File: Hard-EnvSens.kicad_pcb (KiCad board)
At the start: 2 copper layers, 60 x 76.6 mm, 86 parts, among them J2 Conn_01x04_Socket, J3 Conn_02x02_Odd_Even, J4 Conn_01x04_Pin, J5 Conn_02x02_Odd_Even, J6 Conn_01x02_Pin, Q1 SS8050, Q2 SS8050, SW1 SW_Push, U10 BMI160, U3 IP5306, U4 VEML7700-TR, U5 DPS368, U6 SGP41-D-R4, U7 SHT40-AD1B-R2, U8 AS7341-DLGT

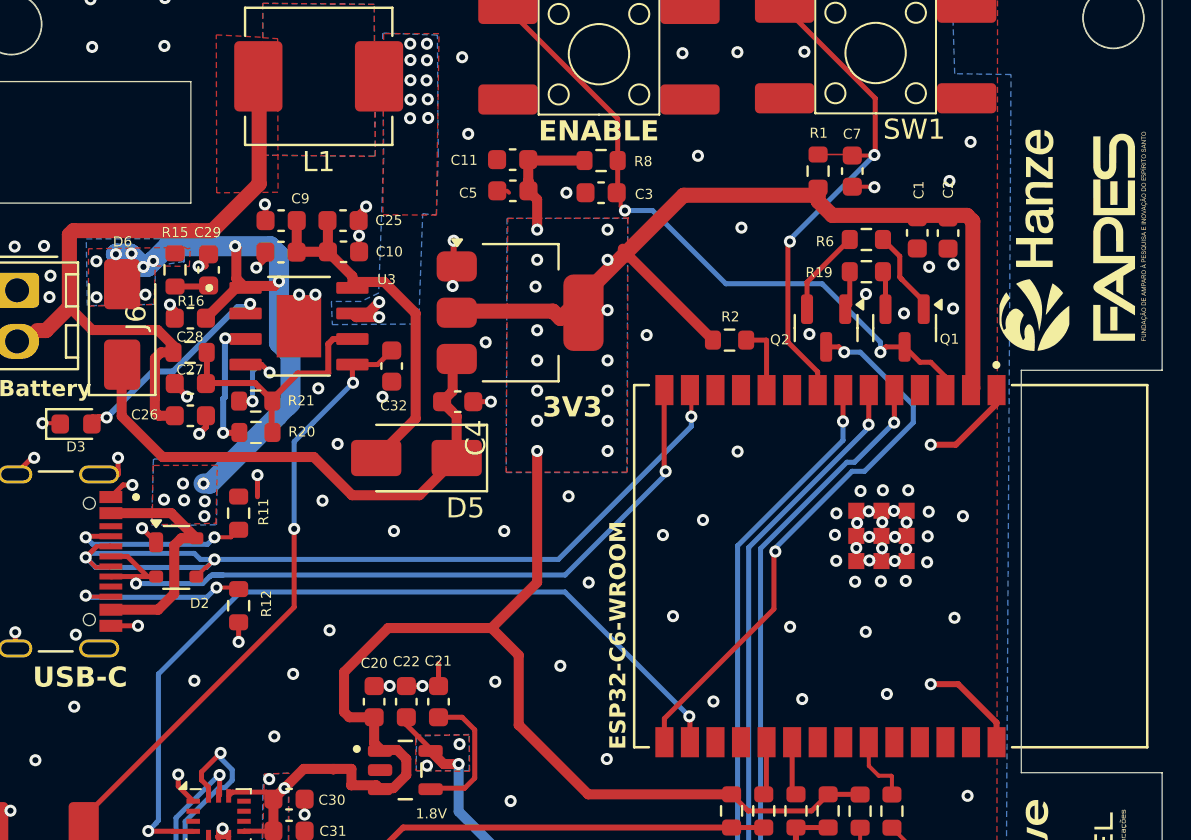
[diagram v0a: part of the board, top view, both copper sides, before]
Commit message: New charger + 3v3 Switch
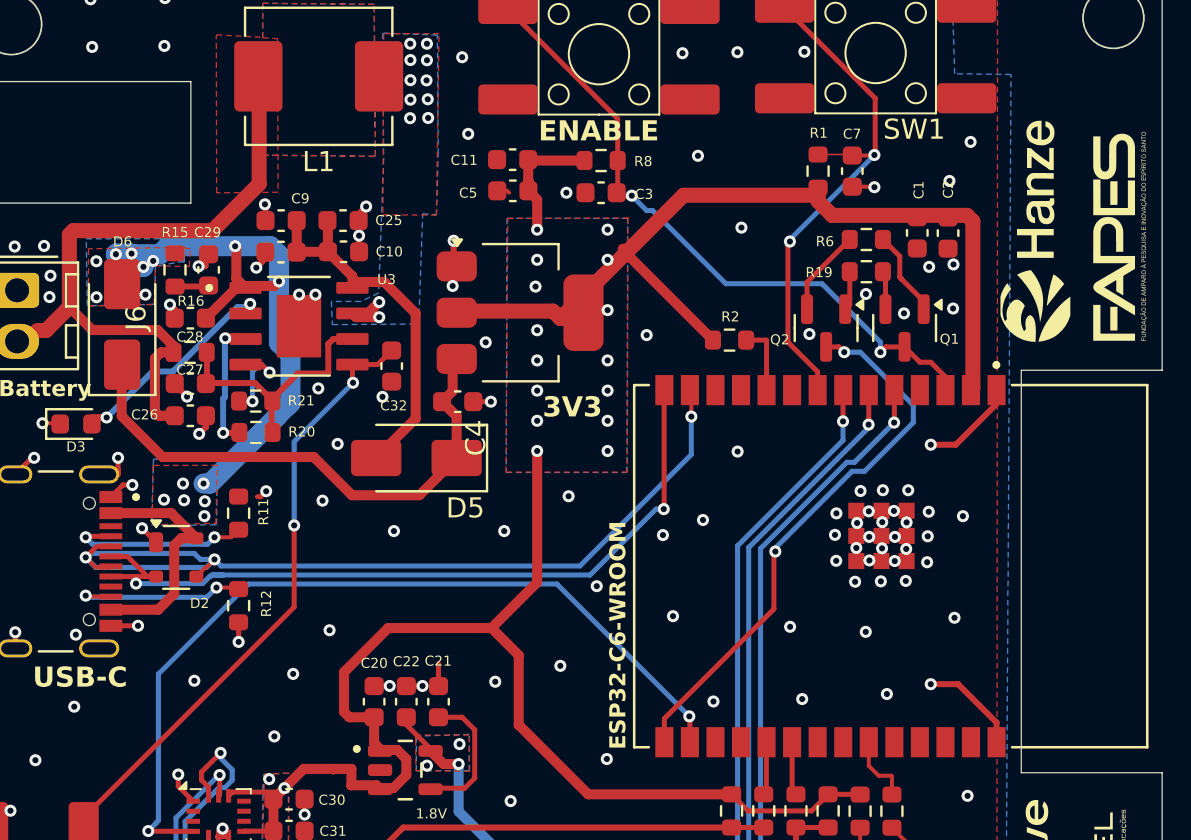
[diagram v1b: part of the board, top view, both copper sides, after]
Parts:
- moved G*** 0.45 mm to (153.8, 63.3)
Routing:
- net +5V: track 41.9 -> 43.2 mm
- net D-: track 46.0 -> 47.1 mm
- net D+: track 38.7 -> 39.6 mm
- net GND: track 42.9 -> 42.4 mm

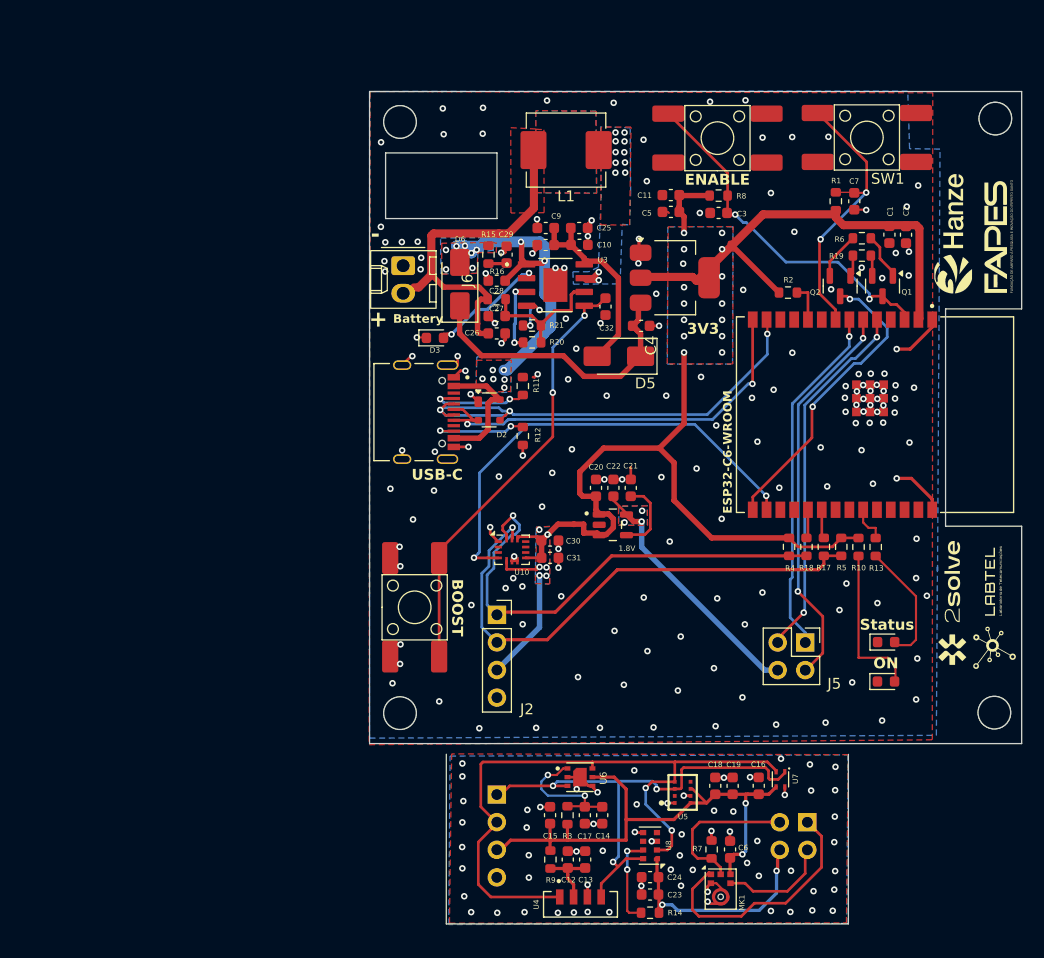
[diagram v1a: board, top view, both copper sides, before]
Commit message: small changes + gotta fix the charger
Maybe rotating the charger 2 gets a better pin configuration
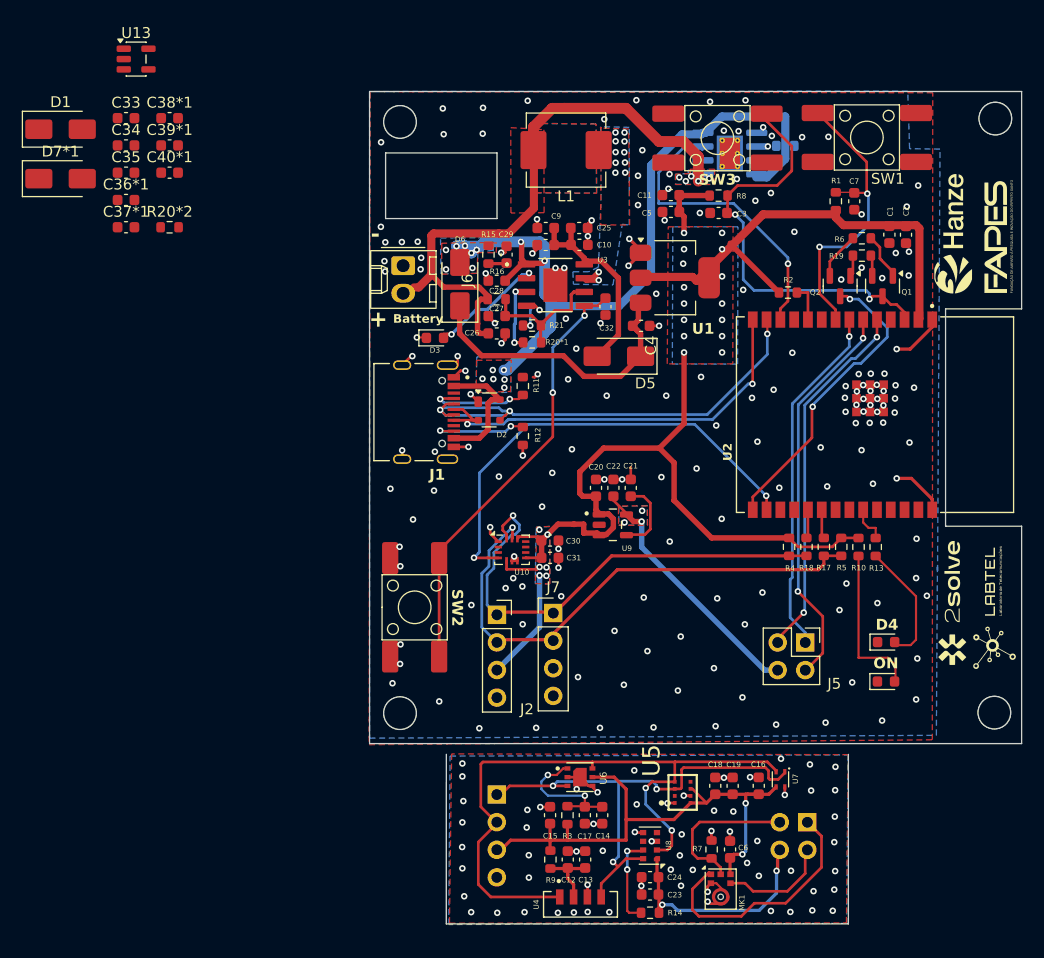
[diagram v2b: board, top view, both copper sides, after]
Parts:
- added C33: 1uF, Capacitor_SMD:C_0603_1608Metric, F.Cu at (77.7, 52.6)
- added C34: 0.1uF, Capacitor_SMD:C_0603_1608Metric, F.Cu at (77.7, 55.2)
- added C35: 1nF, Capacitor_SMD:C_0603_1608Metric, F.Cu at (77.7, 57.7)
- added C36*1: 10uF, Capacitor_SMD:C_0603_1608Metric, F.Cu at (77.7, 60.2)
- added C37*1: 10uF, Capacitor_SMD:C_0603_1608Metric, F.Cu at (77.7, 62.7)
- added C38*1: 10nF, Capacitor_SMD:C_0603_1608Metric, F.Cu at (81.7, 52.6)
- added C39*1: 100uF, Capacitor_SMD:C_0603_1608Metric, F.Cu at (81.7, 55.2)
- added C40*1: 10uF, Capacitor_SMD:C_0603_1608Metric, F.Cu at (81.7, 57.7)
- added D1: SS14, Diode_SMD:D_SMA, F.Cu at (71.7, 53.7)
- added D7*1: SS14, Diode_SMD:D_SMA, F.Cu at (71.7, 58.2)
- added J7: Conn_01x04_Pin, Connector_PinHeader_2.54mm:PinHeader_1x04_P2.54mm_Vertical, F.Cu at (117.0, 98.2)
- added R10*1: 1.2k, Resistor_SMD:R_0603_1608Metric, B.Cu at (138.3, 55.2)
- added R20*2: 0R, Resistor_SMD:R_0603_1608Metric, F.Cu at (81.7, 62.7)
- added U12*1: TP4056-42-ESOP8, Package_SO:SOIC-8-1EP_3.9x4.9mm_P1.27mm_EP2.41x3.3mm_ThermalVias, B.Cu at (133.2, 55.9)
- added U13: SPX3819M5-L-3-3, Package_TO_SOT_SMD:SOT-23-5, F.Cu at (78.6, 47.2)
- U5: footprint Biblioteca_Kicad:LGA8S145X65P2X4_200X250X110-V -> libs:LGA8S145X65P2X4_200X250X110-V
- renumbered Status to D4, USB-C to J1, R20 to R20*1, BOOST to SW2, ENABLE to SW3, 3V3 to U1, ESP32-C6-WROOM to U2, 1.8V to U9
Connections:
- net Net-(J6-Pin_2) renamed Bat+
- C20 pad 1: +3V3 -> 3v3_aux
- C30 pad 1: +3V3 -> 3v3_aux
- C31 pad 1: +3V3 -> 3v3_aux
- J2 pad 3: +3V3 -> 3v3_aux
- R4 pad 2: +3V3 -> 3v3_aux
- R5 pad 2: +3V3 -> 3v3_aux
- SW2 pad 3: Net-(U3-KEY) -> (no net)
- SW2 pad 4: GND -> (no net)
- SW3 pad 3: (no net) -> EN
- U10 pad 5: +3V3 -> 3v3_aux
- U10 pad 8: +3V3 -> 3v3_aux
- U2 pad 12: unconnected-(U2-GPIO11-Pad12) -> Charge_Bat
- U2 pad 17: unconnected-(U2-GPIO19-Pad17) -> Sensors_3v3
- U2 pad 29_1: GND -> (no net)
- U2 pad 29_2: GND -> (no net)
- U2 pad 29_3: GND -> (no net)
- U2 pad 29_4: GND -> (no net)
- U2 pad 29_5: GND -> (no net)
- U2 pad 29_6: GND -> (no net)
- U2 pad 29_7: GND -> (no net)
- U2 pad 29_8: GND -> (no net)
- U2 pad 29_9: GND -> (no net)
- U9 pad 1: +3V3 -> 3v3_aux
- U9 pad 3: +3V3 -> 3v3_aux
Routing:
- net +5V: track 43.2 -> 85.3 mm
- net Charge_Bat: track 0.00 -> 27.9 mm, vias 0 -> 1
- net Bat+: track 32.6 -> 54.7 mm, vias 0 -> 5
- net +3V3: track 129.4 -> 115.1 mm, vias 21 -> 20
- net 3v3_aux: track 0.00 -> 14.3 mm, vias 0 -> 1
- net EN: track 32.8 -> 39.6 mm
- net Net-(U2-GPIO0/ADC1_CH0/XTAL_32K_P): track 26.5 -> 28.2 mm
- net Net-(U12*1-PROG): track 0.00 -> 1.03 mm, vias 0 -> 1
- net GND: track 42.4 -> 42.1 mm, vias 162 -> 172
- added copper zone on B.Cu, net Bat+

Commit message: Almost finished board
New 3v3 regulaator
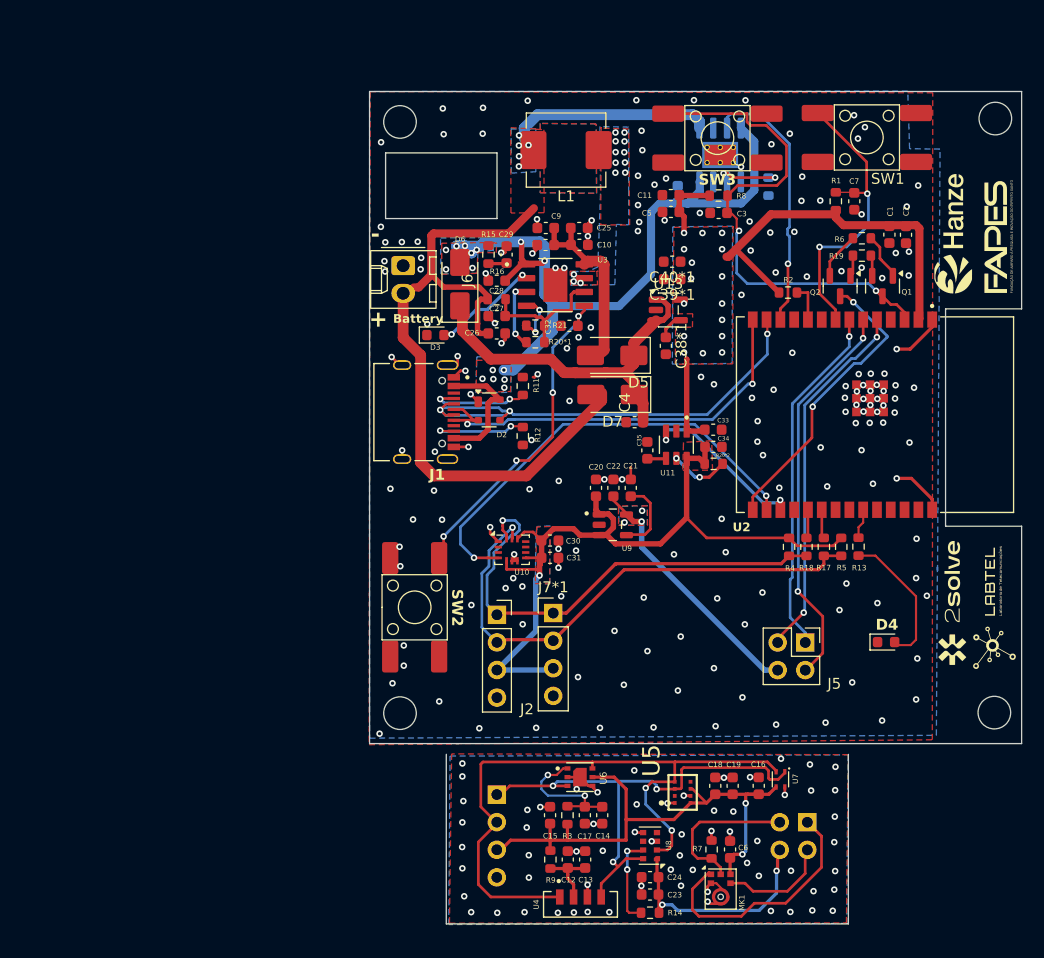
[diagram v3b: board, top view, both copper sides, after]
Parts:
- removed C37*1: 10uF, Capacitor_SMD:C_0603_1608Metric
- removed D1, D7*1: SS14, Diode_SMD:D_SMA
- removed ON: LED, LED_SMD:LED_0603_1608Metric
- removed R10: 1K, Resistor_SMD:R_0603_1608Metric
- removed U1: LD1117S33TR_SOT223, Package_TO_SOT_SMD:SOT-223-3_TabPin2
- added D7: CMS30I30A, Diode_SMD:D_SMA, F.Cu at (122.5, 78.1)
- added U11: TPS22918TDBVRQ1, libs:SOT95P280X145-6N, F.Cu at (128.3, 82.7)
- C36*1: moved to B.Cu
- D5, D6: value SS14 -> CMS30I30A
- moved C33 61.2 mm to (131.7, 81.3)
- moved C34 60.8 mm to (131.7, 82.9)
- moved R20*2 54.6 mm to (131.8, 84.5)
- moved C35 54.4 mm to (125.7, 83.2), turned to 90 degrees
- moved U13 54.1 mm to (127.6, 70.3)
- moved C36*1 50.8 mm to (128.5, 59.6), turned to 90 degrees
- moved C38*1 50.2 mm to (127.4, 73.6), turned to -90 degrees
- moved C39*1 47.9 mm to (128.0, 67.5), turned to 180 degrees
- moved C40*1 47.0 mm to (127.9, 65.9), turned to 180 degrees
- moved C4 8.89 mm to (124.5, 80.6), turned to 180 degrees
- moved R10*1 4.06 mm to (136.8, 59.0), turned to -90 degrees
- moved C32 3.76 mm to (118.5, 71.8), turned to 180 degrees
- moved R13 1.58 mm to (145.1, 92.1)
- moved U12*1 0.90 mm to (132.4, 56.0), turned to 90 degrees
- moved D5 0.62 mm to (122.4, 74.5)
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- renumbered J7 to J7*1
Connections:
- C33 pad 1: Net-(D1-K) -> +3V3
- C39*1 pad 1: 3v3_regulator2 -> +3V3
- C40*1 pad 1: 3v3_regulator2 -> +3V3
- J7*1 pad 2: GND -> Scl
- J7*1 pad 3: Scl -> 3v3_aux
- J7*1 pad 4: +3V3 -> GND
- SW3 pad 3: EN -> (no net)
- U10 pad 12: +3V3 -> 3v3_aux
- U13 pad 1: Bat+ -> Net-(D5-K)
- U13 pad 3: Bat+ -> Net-(D5-K)
- U13 pad 5: 3v3_regulator2 -> +3V3
- U2 pad 29_1: (no net) -> GND
- U2 pad 29_2: (no net) -> GND
- U2 pad 29_3: (no net) -> GND
- U2 pad 29_4: (no net) -> GND
- U2 pad 29_5: (no net) -> GND
- U2 pad 29_6: (no net) -> GND
- U2 pad 29_7: (no net) -> GND
- U2 pad 29_8: (no net) -> GND
- U2 pad 29_9: (no net) -> GND
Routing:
- net +3V3: track 115.1 -> 49.4 mm, vias 20 -> 16
- net 3v3_aux: track 14.3 -> 72.8 mm
- net Bat+: track 54.7 -> 82.7 mm
- net Sensors_3v3: track 0.00 -> 16.1 mm, vias 0 -> 2
- net Net-(D1-A): track 14.5 -> 0.00 mm
- net Net-(U3-KEY): track 40.1 -> 31.1 mm, vias 2 -> 4
- net EN: track 39.6 -> 47.5 mm
- net Net-(D5-K): track 28.6 -> 34.5 mm
- net +5V: track 85.3 -> 79.5 mm
- net GND: track 42.1 -> 36.4 mm, vias 172 -> 175
- net Net-(U11-QOD): track 0.00 -> 5.48 mm, vias 0 -> 2
- net Net-(U12*1-PROG): track 1.03 -> 6.14 mm, vias 1 -> 2
- net Charge_Bat: track 27.9 -> 24.7 mm
- net Net-(U3-SW): track 2.98 -> 0.00 mm, vias 12 -> 13
- net Net-(U13-BP): track 0.00 -> 2.47 mm
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- added copper zone on B.Cu, net 3v3_aux
- added copper zone on F.Cu, net 3v3_aux

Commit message: Almost ready to fabricate
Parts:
- added R32*1: 10k, Resistor_SMD:R_0603_1608Metric, B.Cu at (140.1, 62.6)
- C39: renamed from C39*1; footprint Capacitor_SMD:C_0603_1608Metric -> Capacitor_SMD:C_Elec_6.3x7.7
- C40: renamed from C40*1; value 10uF -> 0.1uF
- R31*1: renamed from R10*1; value 1.2k -> 4k
- moved C39 7.83 mm to (129.7, 75.1), turned to -90 degrees
- moved C38 3.29 mm to (126.9, 70.3), turned to 180 degrees
- moved U13 2.57 mm to (127.4, 67.7)
- moved C40 0.62 mm to (127.9, 65.2)
- moved J7*1 0.18 mm to (117.0, 98.4)
- renumbered C38*1 to C38, R20*2 to R30*1
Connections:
- U2 pad 29_1: GND -> (no net)
- U2 pad 29_2: GND -> (no net)
- U2 pad 29_3: GND -> (no net)
- U2 pad 29_4: GND -> (no net)
- U2 pad 29_5: GND -> (no net)
- U2 pad 29_6: GND -> (no net)
- U2 pad 29_7: GND -> (no net)
- U2 pad 29_8: GND -> (no net)
- U2 pad 29_9: GND -> (no net)
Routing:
- net GND: track 36.4 -> 30.0 mm, vias 175 -> 253
- net +3V3: track 49.4 -> 51.9 mm, vias 16 -> 17
- net Net-(D5-K): track 34.5 -> 36.7 mm
- net Net-(U11-QOD): track 5.48 -> 7.54 mm
- net 3v3_aux: track 72.8 -> 74.6 mm
- net Charge_Bat: track 24.7 -> 25.9 mm
- net GND2: vias 64 -> 76
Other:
- outline, holes or cut-outs redrawn
- board text added: "STATUS"

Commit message: ready to fabricate
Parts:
- added 1V8: TestPoint, TestPoint:TestPoint_THTPad_1.5x1.5mm_Drill0.7mm, F.Cu at (149.3, 106.6)
- added 3V3: TestPoint, TestPoint:TestPoint_THTPad_1.5x1.5mm_Drill0.7mm, F.Cu at (145.5, 103.5)
- added ?: , , F.Cu at (157.6, 107.3)
- added ?: , , F.Cu at (102.9, 53.0)
- added ?: , , F.Cu at (102.9, 107.4)
- added Bat: TestPoint, TestPoint:TestPoint_THTPad_1.5x1.5mm_Drill0.7mm, F.Cu at (145.5, 106.7)
- added Boost: TestPoint, TestPoint:TestPoint_THTPad_1.5x1.5mm_Drill0.7mm, F.Cu at (145.5, 100.3)
- added GND: TestPoint, TestPoint:TestPoint_THTPad_1.5x1.5mm_Drill0.7mm, F.Cu at (153.0, 106.6)
- added REF**: Hole 3mm, libs:Hole 3mm, F.Cu at (157.7, 52.7)
- added RX: TestPoint, TestPoint:TestPoint_THTPad_1.5x1.5mm_Drill0.7mm, F.Cu at (149.3, 97.1)
- added Sensor: TestPoint, TestPoint:TestPoint_THTPad_1.5x1.5mm_Drill0.7mm, F.Cu at (149.3, 103.5)
- added TX: TestPoint, TestPoint:TestPoint_THTPad_1.5x1.5mm_Drill0.7mm, F.Cu at (145.6, 97.1)
- added Usb: TestPoint, TestPoint:TestPoint_THTPad_1.5x1.5mm_Drill0.7mm, F.Cu at (149.3, 100.3)
- moved D4 46.5 mm to (102.8, 88.3), turned to -90 degrees
- moved R7 8.26 mm to (123.4, 121.0)
- moved C19 8.26 mm to (125.3, 115.2)
- moved C6 8.26 mm to (125.1, 121.0)
- moved C13 8.26 mm to (111.7, 122.0)
- moved C14 8.26 mm to (113.3, 117.9)
- moved C15 8.26 mm to (108.5, 117.9)
- moved C17 8.26 mm to (111.7, 117.9)
- moved C23 8.26 mm to (117.7, 125.2)
- moved C24 8.26 mm to (117.7, 123.6)
- moved J3 8.26 mm to (132.2, 118.5)
- moved J4 8.26 mm to (103.6, 116.0)
- moved R14 8.26 mm to (117.7, 126.8)
- moved R3 8.26 mm to (110.1, 117.9)
- moved R9 8.26 mm to (108.5, 122.0)
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- renumbered J7*1 to J7, R20*1 to R20
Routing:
- net +5V: track 79.5 -> 149.3 mm, vias 15 -> 16
- net +5vBat: track 17.4 -> 64.9 mm, vias 0 -> 3
- net Bat+: track 82.7 -> 123.7 mm, vias 5 -> 7
- net +3V3: track 51.9 -> 88.7 mm, vias 17 -> 18
- net Net-(D4-A): track 13.0 -> 48.4 mm, vias 0 -> 2
- net +1V8: track 23.4 -> 36.5 mm
- net 3v3_aux: track 74.6 -> 87.6 mm, vias 1 -> 2
- net RX: track 0.00 -> 8.93 mm
- net TX: track 0.00 -> 8.91 mm
- net GND: track 30.0 -> 30.5 mm, vias 253 -> 271
- net GND2: vias 76 -> 75
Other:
- board size 60 x 76.6 mm -> 60 x 77.7 mm
- board text added: "Test Points"

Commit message: ready to fabricate
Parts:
- ON / OFF: renamed from SW2
- moved C7 0.26 mm to (144.7, 60.6)
- moved R1 0.26 mm to (143.0, 60.6)
- moved ON / OFF 0.21 mm to (104.1, 97.7)
- renumbered SW1 to BOOT, SW3 to Enable, MK1 to MIC, R30*1 to R30
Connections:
- U2 pad 29_1: (no net) -> GND
- U2 pad 29_2: (no net) -> GND
- U2 pad 29_3: (no net) -> GND
- U2 pad 29_4: (no net) -> GND
- U2 pad 29_5: (no net) -> GND
- U2 pad 29_6: (no net) -> GND
- U2 pad 29_7: (no net) -> GND
- U2 pad 29_8: (no net) -> GND
- U2 pad 29_9: (no net) -> GND
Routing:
- net GND2: track 24.5 -> 24.1 mm, vias 75 -> 77
- net GND: track 30.5 -> 30.6 mm, vias 271 -> 272
- net +3V3: vias 18 -> 15
